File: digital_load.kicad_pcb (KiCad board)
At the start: 4 copper layers, 50 x 50 mm, 76 parts, among them J1 Conn_01x02, J2 USB_C_Receptacle_USB2.0, J3 Conn_01x10, J301 Conn_PIC_ICSP_ICD, J4 Conn_01x10, Q501 IPA60R800CE, Q502 Q_NMOS_GSD, Q503 Q_NMOS_GSD, Q504 Q_NMOS_GSD, SW601 PEC11R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

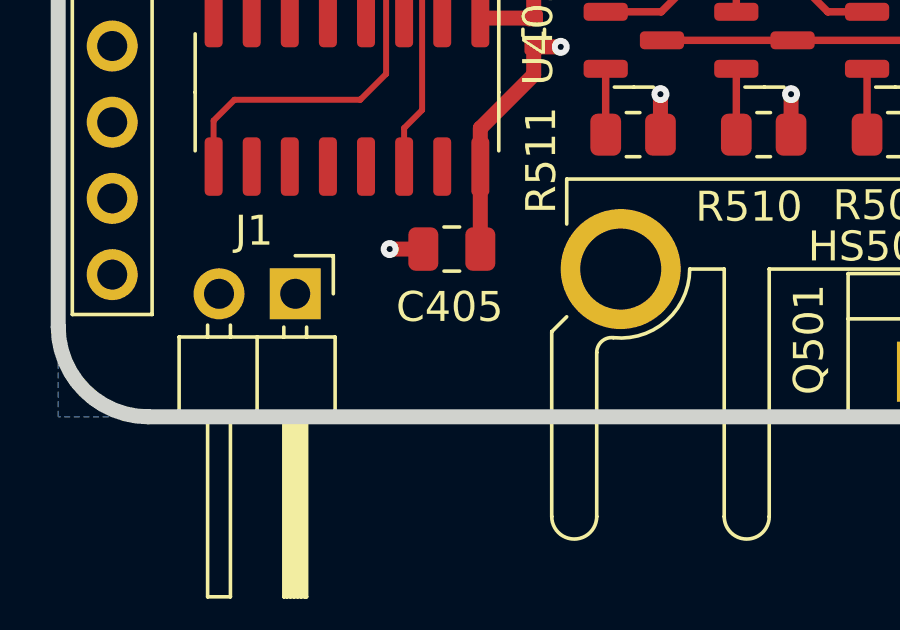
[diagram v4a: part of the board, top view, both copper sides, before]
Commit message: Change some partnumbers in preparation for the order
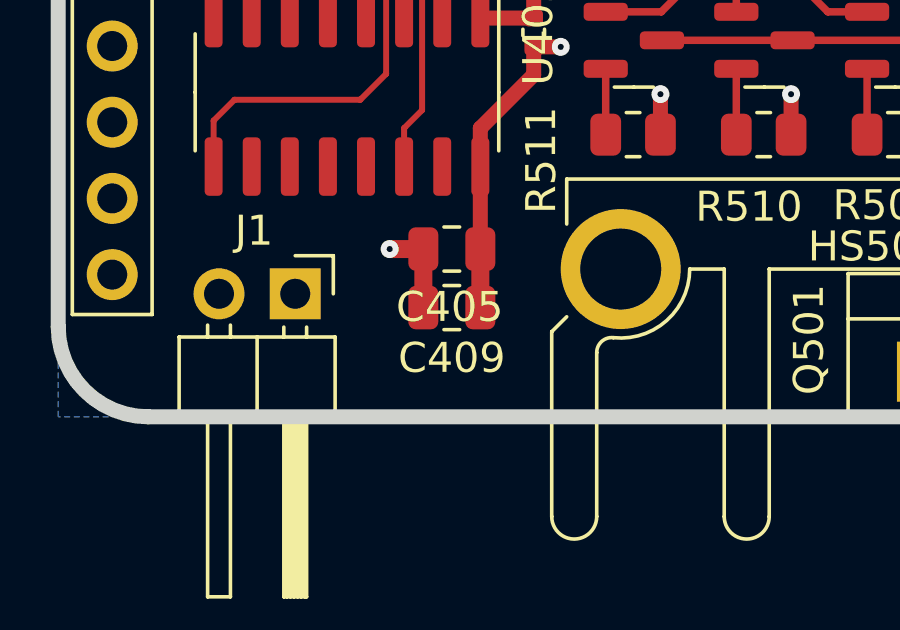
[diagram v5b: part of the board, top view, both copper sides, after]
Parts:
- added C409: 4.7u, Capacitor_SMD:C_0805_2012Metric, F.Cu at (113.1, 126.4)
- C405, C501: value 10u -> 4.7u
- Q501: value IPA60R800CE -> IRLS640A
- R506: value 5M -> 4.7M
- R507: value 50k -> 47k
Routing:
- net GND: track 70.2 -> 72.2 mm
- net +5V: track 23.4 -> 25.4 mm
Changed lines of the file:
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@@
   (net 72 "unconnected-(U402-Pad15)")
   (net 73 "unconnected-(U701-Pad5)")
-  (net 74 "Net-(U701-Pad7)")
+  (net 74 "Net-(R702-Pad2)")
   (net 75 "unconnected-(U701-Pad2)")
   (net 76 "unconnected-(U701-Pad6)")
@@
       (effects (font (size 1 1) (thickness 0.15)))
     )
-    (fp_text value "10u" (at 0 1.68 90) (layer "F.Fab")
+    (fp_text value "4.7u" (at 0 1.68 90) (layer "F.Fab")
       (effects (font (size 1 1) (thickness 0.15)))
     )
@@
     (fp_line (start 1 0.625) (end -1 0.625) (layer "F.Fab") (width 0.1))
     (pad "1" smd roundrect locked (at -0.9125 0 180) (size 1.025 1.4) (layers "F.Cu" "F.Paste" "F.Mask") (roundrect_rratio 0.243902)
-      (net 74 "Net-(U701-Pad7)") (pintype "passive"))
+      (net 74 "Net-(R702-Pad2)") (pintype "passive"))
     (pad "2" smd roundrect locked (at 0.9125 0 180) (size 1.025 1.4) (layers "F.Cu" "F.Paste" "F.Mask") (roundrect_rratio 0.243902)
       (net 2 "GND") (pintype "passive"))
@@
       (effects (font (size 1 1) (thickness 0.15)))
     )
-    (fp_text value "50k" (at 0 1.65) (layer "F.Fab")
+    (fp_text value "47k" (at 0 1.65) (layer "F.Fab")
       (effects (font (size 1 1) (thickness 0.15)))
     )
@@
     (tags "SOIC SO")
     (property "Manufacturer" "Texas Instrument")
-    (property "PartNumber" "LP2951-33D")
+    (property "PartNumber" "LP2951-30D")
     (property "Sheetfile" "power.kicad_sch")
     (property "Sheetname" "Power")
@@
       (net 76 "unconnected-(U701-Pad6)") (pinfunction "VTAP") (pintype "input+no_connect"))
     (pad "7" smd roundrect locked (at 2.475 -0.635 90) (size 1.95 0.6) (layers "F.Cu" "F.Paste" "F.Mask") (roundrect_rratio 0.25)
-      (net 74 "Net-(U701-Pad7)") (pinfunction "FEEDBACK") (pintype "input"))
+      (net 74 "Net-(R702-Pad2)") (pinfunction "FEEDBACK") (pintype "input"))
     (pad "8" smd roundrect locked (at 2.475 -1.905 90) (size 1.95 0.6) (layers "F.Cu" "F.Paste" "F.Mask") (roundrect_rratio 0.25)
       (net 19 "+5V") (pinfunction "IN") (pintype "power_in"))
@@
   )
   (footprint "Capacitor_SMD:C_0805_2012Metric" (layer "F.Cu")
+    (at 113.119975 126.359547 180)
+    (descr "Capacitor SMD 0805 (2012 Metric), square (rectangular) end terminal, IPC_7351 nominal, (Body size source: IPC-SM-782 page 76, https://www.pcb-3d.com/wordpress/wp-content/uploads/ipc-sm-782a_amendment_1_and_2.pdf, https://docs.google.com/spreadsheets/d/1BsfQQcO9C6DZCsRaXUlFlo91Tg2WpOkGARC1WS5S8t0/edit?usp=sharing), generated with kicad-footprint-generator")
+    (tags "capacitor")
+    (property "Manufacturer" "Generic")
+    (property "PartNumber" "Generic")
+    (property "Sheetfile" "usb_uart.kicad_sch")
+    (property "Sheetname" "usb_uart")
+    (property "exclude_from_bom" "")
+    (attr smd exclude_from_bom)
+    (fp_text reference "C409" (at 0 -1.68) (layer "F.SilkS")
+      (effects (font (size 1 1) (thickness 0.15)))
+    )
+    (fp_text value "4.7u" (at 0 1.68) (layer "F.Fab")
+      (effects (font (size 1 1) (thickness 0.15)))
+    )
+    (fp_text user "${REFERENCE}" (at 0 0) (layer "F.Fab")
+      (effects (font (size 0.5 0.5) (thickness 0.08)))
+    )
+    (fp_line (start -0.261252 0.735) (end 0.261252 0.735) (layer "F.SilkS") (width 0.12))
+    (fp_line (start -0.261252 -0.735) (end 0.261252 -0.735) (layer "F.SilkS") (width 0.12))
+    (fp_line (start -1.7 -0.98) (end 1.7 -0.98) (layer "F.CrtYd") (width 0.05))
+    (fp_line (start -1.7 0.98) (end -1.7 -0.98) (layer "F.CrtYd") (width 0.05))
+    (fp_line (start 1.7 0.98) (end -1.7 0.98) (layer "F.CrtYd") (width 0.05))
+    (fp_line (start 1.7 -0.98) (end 1.7 0.98) (layer "F.CrtYd") (width 0.05))
+    (fp_line (start 1 0.625) (end -1 0.625) (layer "F.Fab") (width 0.1))
+    (fp_line (start -1 -0.625) (end 1 -0.625) (layer "F.Fab") (width 0.1))
+    (fp_line (start -1 0.625) (end -1 -0.625) (layer "F.Fab") (width 0.1))
+    (fp_line (start 1 -0.625) (end 1 0.625) (layer "F.Fab") (width 0.1))
+    (pad "1" smd roundrect (at -0.95 0 180) (size 1 1.45) (layers "F.Cu" "F.Paste" "F.Mask") (roundrect_rratio 0.25)
+      (net 19 "+5V") (pintype "passive"))
+    (pad "2" smd roundrect (at 0.95 0 180) (size 1 1.45) (layers "F.Cu" "F.Paste" "F.Mask") (roundrect_rratio 0.25)
+      (net 2 "GND") (pintype "passive"))
+    (model "${KICAD6_3DMODEL_DIR}/Capacitor_SMD.3dshapes/C_0805_2012Metric.wrl"
+      (offset (xyz 0 0 0))
+      (scale (xyz 1 1 1))
+      (rotate (xyz 0 0 0))
+    )
+  )
+  (footprint "Capacitor_SMD:C_0805_2012Metric" (layer "F.Cu")
     (at 113.119975 124.408186 180)
     (descr "Capacitor SMD 0805 (2012 Metric), square (rectangular) end terminal, IPC_7351 nominal, (Body size source: IPC-SM-782 page 76, https://www.pcb-3d.com/wordpress/wp-content/uploads/ipc-sm-782a_amendment_1_and_2.pdf, https://docs.google.com/spreadsheets/d/1BsfQQcO9C6DZCsRaXUlFlo91Tg2WpOkGARC1WS5S8t0/edit?usp=sharing), generated with kicad-footprint-generator")
@@
       (effects (font (size 1 1) (thickness 0.15)))
     )
-    (fp_text value "10u" (at 0 1.68) (layer "F.Fab")
+    (fp_text value "4.7u" (at 0 1.68) (layer "F.Fab")
       (effects (font (size 1 1) (thickness 0.15)))
     )
@@
     (fp_arc (start 15 8.25) (mid 14.25 9) (end 13.5 8.25) (layer "F.CrtYd") (width 0.05))
     (fp_arc (start -10.4 0) (mid -11.162952 1.711583) (end -12.946427 2.286761) (layer "F.CrtYd") (width 0.05))
-    (fp_arc (start 12.453571 2.286756) (mid 13.199861 2.669068) (end 13.5 3.45201) (layer "F.CrtYd") (width 0.05))
+    (fp_arc (start 12.453571 2.286756) (mid 13.199858 2.66906) (end 13.5 3.45201) (layer "F.CrtYd") (width 0.05))
     (fp_arc (start 9.25 8.25) (mid 8.5 9) (end 7.75 8.25) (layer "F.CrtYd") (width 0.05))
     (fp_arc (start -13.5 2.78388) (mid -13.334141 2.411796) (end -12.946429 2.286758) (layer "F.CrtYd") (width 0.05))
@@
       (net 3 "+3V3") (pintype "passive"))
     (pad "2" smd roundrect locked (at 0.9125 0 180) (size 1.025 1.4) (layers "F.Cu" "F.Paste" "F.Mask") (roundrect_rratio 0.243902)
-      (net 74 "Net-(U701-Pad7)") (pintype "passive"))
+      (net 74 "Net-(R702-Pad2)") (pintype "passive"))
     (model "${KICAD6_3DMODEL_DIR}/Resistor_SMD.3dshapes/R_0805_2012Metric.wrl"
       (offset (xyz 0 0 0))
@@
     (descr "TO-220-3, Vertical, RM 2.54mm, see https://www.vishay.com/docs/66542/to-220-1.pdf")
     (tags "TO-220-3 Vertical RM 2.54mm")
-    (property "Manufacturer" "Infineon")
-    (property "PartNumber" "IPA60R800CE")
+    (property "Manufacturer" "On Semiconductor")
+    (property "PartNumber" "IRLS640A")
     (property "Sheetfile" "load_control.kicad_sch")
     (property "Sheetname" "load_control")
@@
       (effects (font (size 1 1) (thickness 0.15)))
     )
-    (fp_text value "IPA60R800CE" (at 2.54 2.5) (layer "F.Fab")
+    (fp_text value "IRLS640A" (at 2.54 2.5) (layer "F.Fab")
       (effects (font (size 1 1) (thickness 0.15)))
     )
@@
       (effects (font (size 1 1) (thickness 0.15)))
     )
-    (fp_text value "5M" (at 0 1.65) (layer "F.Fab")
+    (fp_text value "4.7M" (at 0 1.65) (layer "F.Fab")
       (effects (font (size 1 1) (thickness 0.15)))
     )
@@
     (property "Sheetfile" "usb_uart.kicad_sch")
     (property "Sheetname" "usb_uart")
-    (attr smd)
+    (property "exclude_from_bom" "")
+    (attr smd exclude_from_bom)
     (fp_text reference "U402" (at -2.033666 -6.375025 90) (layer "F.SilkS")
       (effects (font (size 1 1) (thickness 0.15)))
@@
   (segment (start 129.868409 93.440157) (end 127.7425 93.440157) (width 0.5) (layer "F.Cu") (net 2))
   (segment (start 104.752598 108.395509) (end 104.752598 107.503759) (width 0.25) (layer "F.Cu") (net 2))
+  (segment (start 112.169975 126.359547) (end 112.169975 124.408186) (width 0.6) (layer "F.Cu") (net 2))
   (segment (start 116.174937 108.445) (end 116.174937 107.558017) (width 0.25) (layer "F.Cu") (net 2))
   (segment (start 107.7575 88.0125) (end 111.3125 88.0125) (width 0.6) (layer "F.Cu") (net 2))
@@
   (segment (start 135.947088 113.210492) (end 135.947088 112.62448) (width 0.25) (layer "F.Cu") (net 2))
   (segment (start 106.867564 106.82) (end 105.742564 106.82) (width 0.25) (layer "F.Cu") (net 2))
-  (segment (start 111.048743 124.408186) (end 112.169975 124.408186) (width 0.5) (layer "F.Cu") (net 2))
+  (segment (start 111.048743 124.408186) (end 112.169975 124.408186) (width 0.6) (layer "F.Cu") (net 2))
   (segment (start 103.815301 105.025) (end 104.742139 105.025) (width 0.25) (layer "F.Cu") (net 2))
   (segment (start 116.08692 107.47) (end 116.174937 107.558017) (width 0.2) (layer "F.Cu") (net 2))
@@
   (segment locked (start 127.3875 102.645099) (end 128.633134 102.645099) (width 0.2) (layer "F.Cu") (net 18))
   (segment (start 136.175 82.4) (end 132.8029 85.7721) (width 0.6) (layer "F.Cu") (net 18))
+  (segment (start 114.069975 126.359547) (end 114.069975 124.408186) (width 0.6) (layer "F.Cu") (net 19))
   (segment (start 139.693095 118.375) (end 137.966572 118.375) (width 0.5) (layer "F.Cu") (net 19))
   (segment (start 105.976799 98.667338) (end 106.867908 98.667338) (width 0.5) (layer "F.Cu") (net 19))

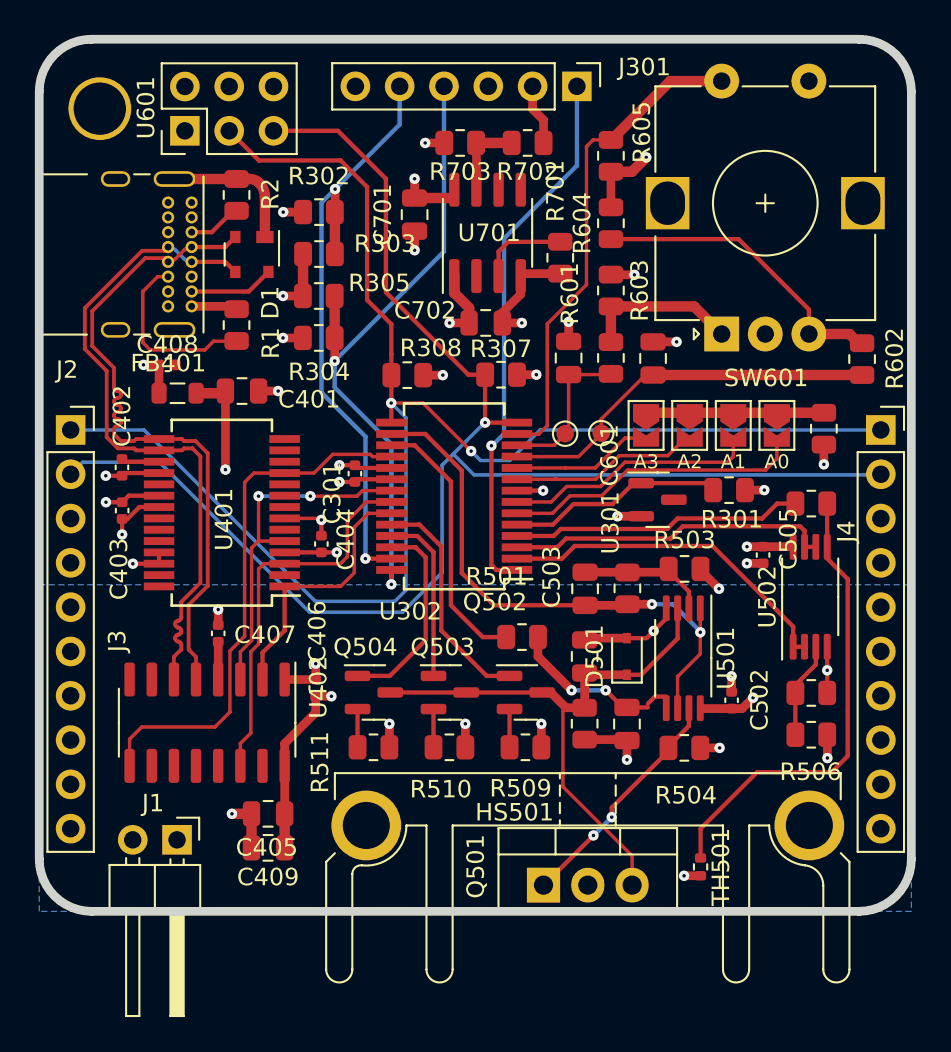
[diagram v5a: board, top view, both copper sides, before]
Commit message: Unclutter silk screen
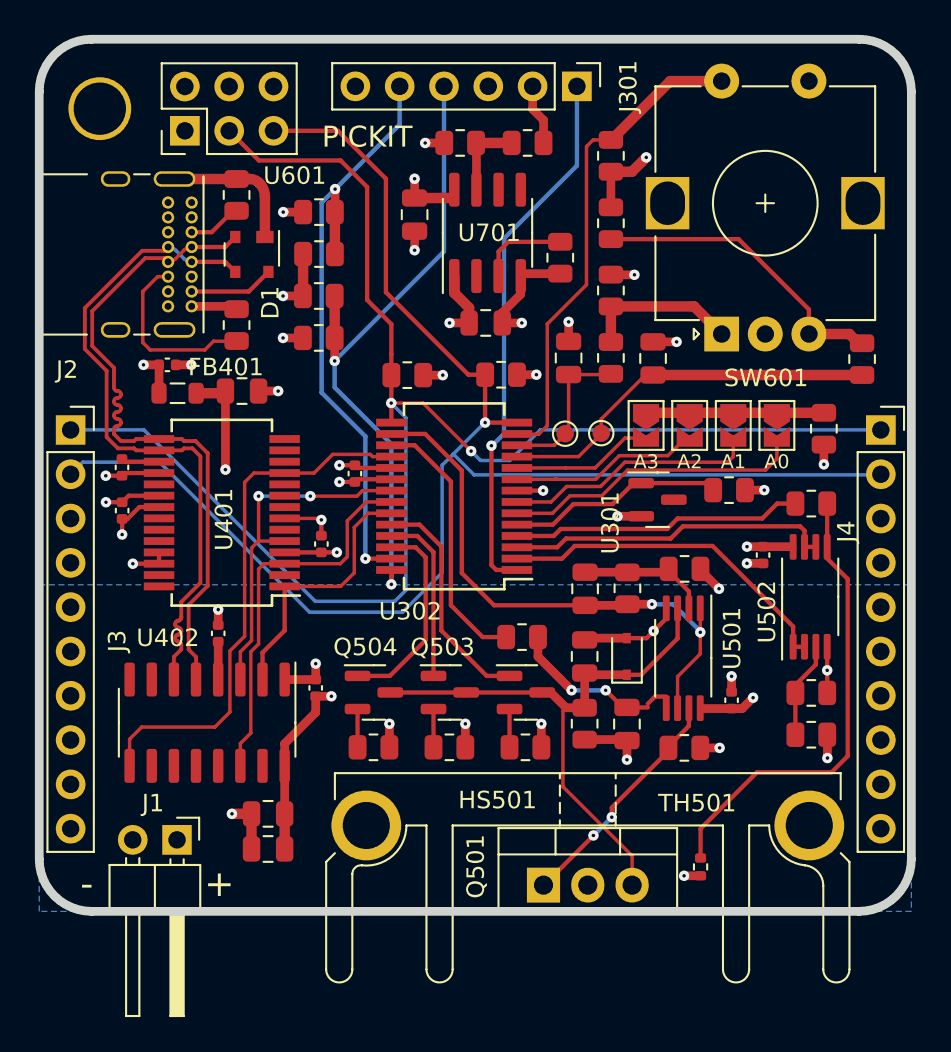
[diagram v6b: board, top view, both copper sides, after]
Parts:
- moved C409 0.07 mm to (113.1, 126.4)
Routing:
- net GND: track 72.2 -> 73.1 mm, vias 28 -> 29
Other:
- board text added: "+"
- board text added: "+++----"
- board text added: "+5V"
- board text added: "-"
- board text added: "PICKIT"
- board text added: "SCL"
- board text added: "SDA"

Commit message: Reduce trace resistance of 10mOhm channel
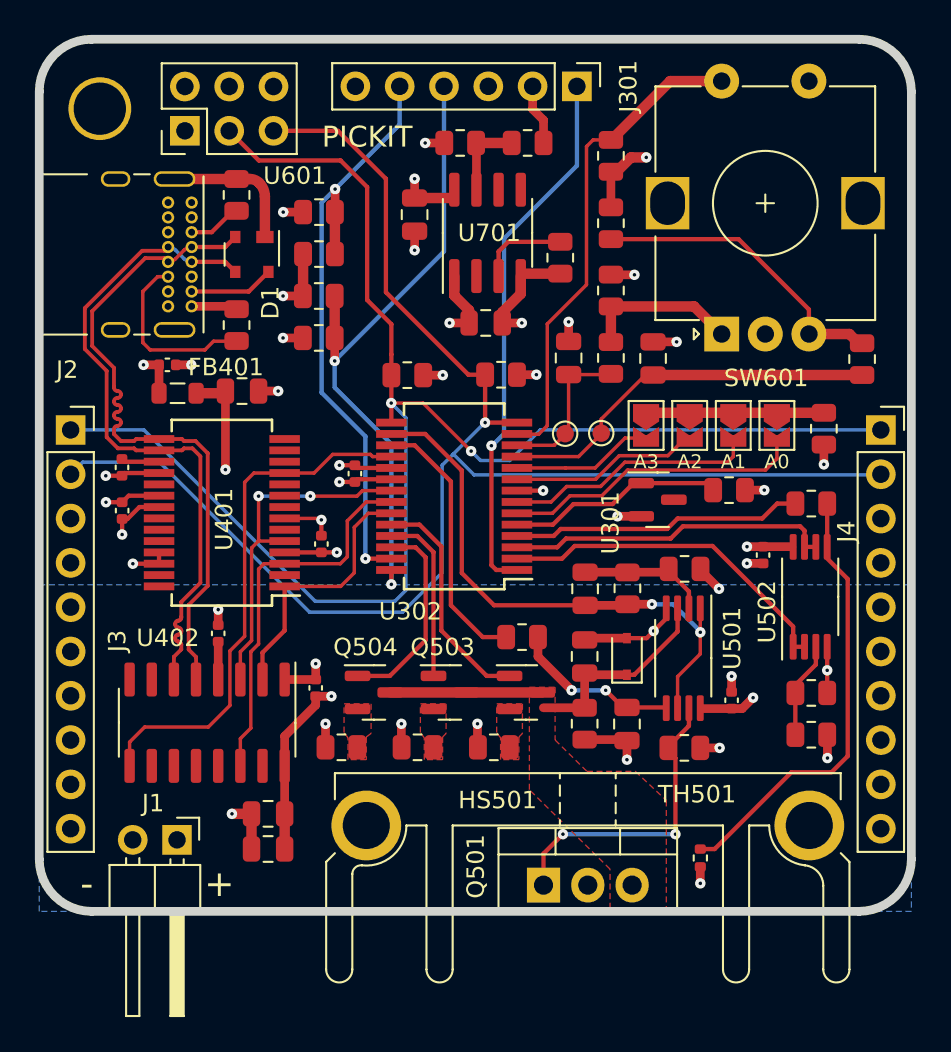
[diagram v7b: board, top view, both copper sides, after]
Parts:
- moved R509 10.5 mm to (117.3, 120.6), turned to 0 degrees
- moved R511 6.90 mm to (126.1, 120.6), turned to 0 degrees
- moved R510 1.83 mm to (121.7, 120.6), turned to 0 degrees
- moved TH501 0.51 mm to (137.9, 126.9)
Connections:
- R509 pad 2: Net-(Q502-Pad2) -> Net-(Q504-Pad2)
- R511 pad 2: Net-(Q504-Pad2) -> Net-(Q502-Pad2)
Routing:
- net /load_control/current_sense: track 32.6 -> 21.2 mm
- net Net-(Q501-Pad1): track 13.6 -> 17.7 mm
- net Net-(Q504-Pad2): track 2.19 -> 0.00 mm
- net Net-(Q503-Pad2): track 2.19 -> 0.00 mm
- net Net-(Q502-Pad2): track 2.19 -> 0.00 mm
- net Net-(R508-Pad2): track 26.4 -> 25.2 mm
- added copper zone on F.Cu, net /load_control/current_sense
- added copper zone on F.Cu, net Net-(Q502-Pad2)
- added copper zone on F.Cu, net Net-(Q503-Pad2)
- added copper zone on F.Cu, net Net-(Q504-Pad2)
